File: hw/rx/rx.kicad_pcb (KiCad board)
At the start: 4 copper layers, 48 x 90 mm, 117 parts, among them J1 backplane 2x13, J2 SWD, J3 ANT_A, J4 ANT_B, J5 TO_MODULE, K1 TQ2SA-12V, Q1 BSS138, U1 BT40E, U2 PE4259, U3 PCM5102A, U4 TLV76733, U5 TLV76733, U6 OPA1656, U7 TPS3808G01

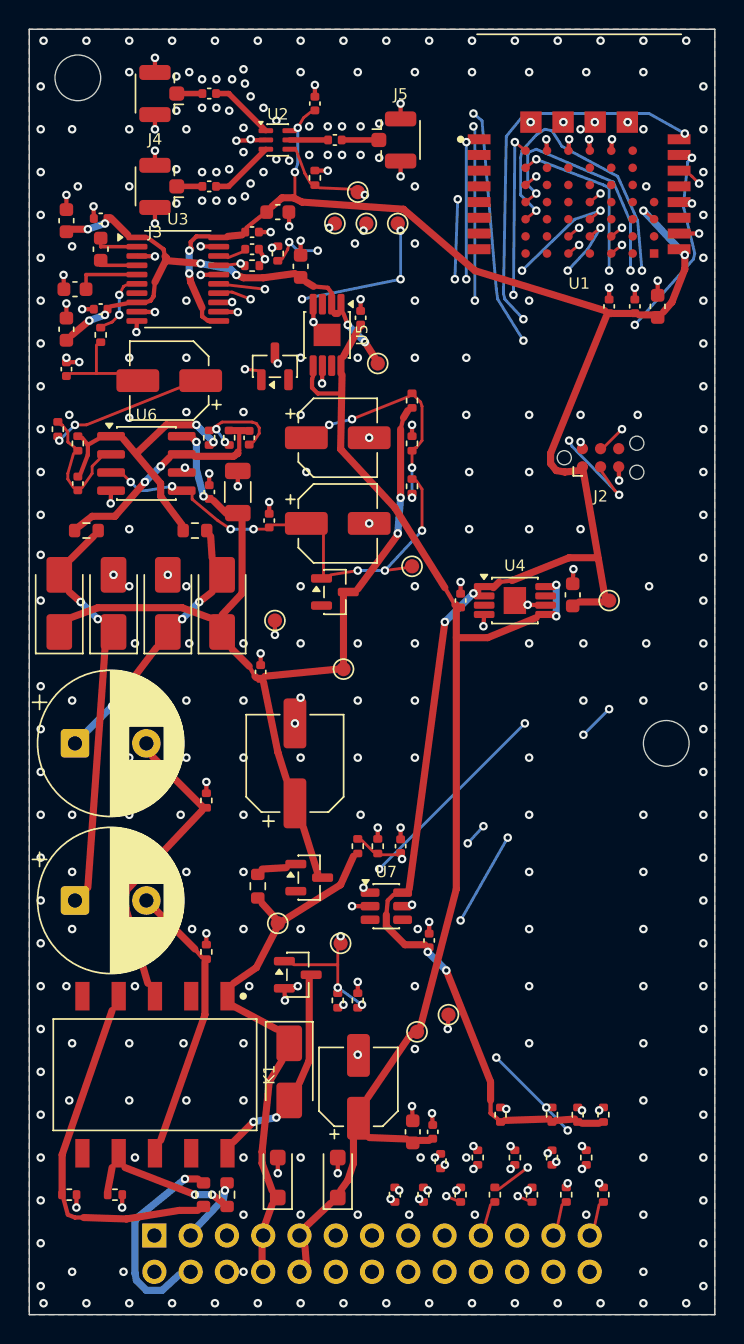
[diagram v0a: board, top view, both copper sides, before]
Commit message: hw/rx: field-solved 50 ohm GCPW, JLC rules that actually load (pack too), rx layout tests + CI (#34)
- rf_line.py: 2D quasi-static solve of the L1/L2 coplanar line; w 0.31 / gap 0.25 -> 50.1 ohm
  (the closed-form CPW formula misses by +7 ohm for gap > h)
- .kicad_dru: KiCad 10 drops the whole file on min_resolved_spokes; removed in pack and rx, guard tests added
- zone fill saved from kicad-cli (netclass RF gap reaches the gerbers)
- tests/test_rx_layout.py: DRC, rules loaded, fresh outputs, pad parity, RF width, current paths, analog keep-out,
  LCSC/DNP coverage, CPL rotations, mech record; CI pcb job runs it

Co-Authored-By: Claude Opus 5.5 <noreply@anthropic.com>
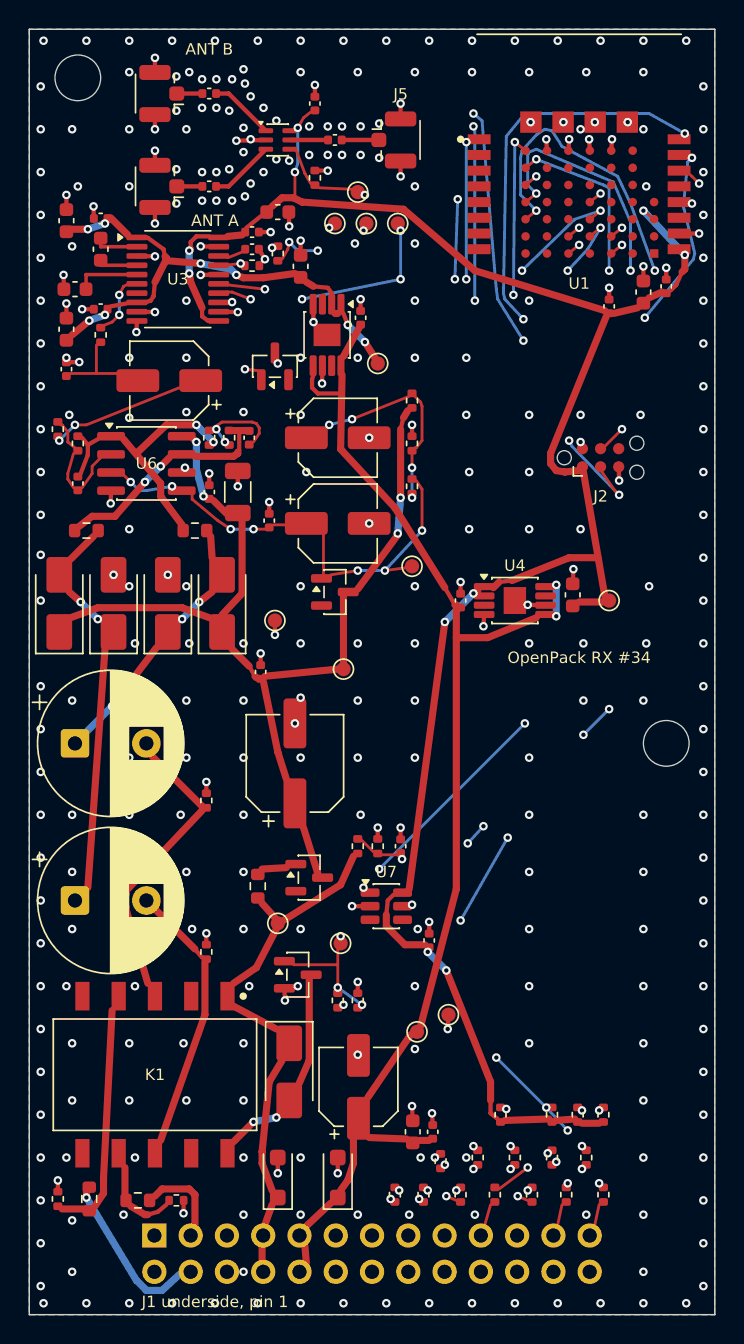
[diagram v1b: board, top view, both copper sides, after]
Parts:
- moved R48 8.01 mm to (104.2, 91.9)
- moved R51 6.26 mm to (107.6, 92.0), turned to 0 degrees
- moved R52 4.32 mm to (110.3, 92.0)
- moved C11 2.61 mm to (144.6, 28.0)
- moved C10 1.41 mm to (143.0, 28.4)
- moved R49 0.85 mm to (102.0, 91.9), turned to 90 degrees
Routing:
- net DRV_COLD_O: track 23.5 -> 15.4 mm
- net DRV_HOT_O: track 8.94 -> 4.78 mm, vias 2 -> 0
- net AUD_COLD: track 13.4 -> 10.9 mm
- net AUD_HOT: track 3.43 -> 5.27 mm, vias 1 -> 0
- net +3V3: track 131.8 -> 130.9 mm
- net GND: track 62.2 -> 62.1 mm, vias 334 -> 336
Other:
- board text added: "ANT A"
- board text added: "ANT B"
- board text added: "J1 underside, pin 1"
- board text added: "OpenPack RX #34"

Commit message: hw/rx: decoupling caps to their pins (op-amp V+ 1.9 mm, LDO in/out swapped to the right sides, supervisor) (#34)
Co-Authored-By: Claude Opus 5.5 <noreply@anthropic.com>
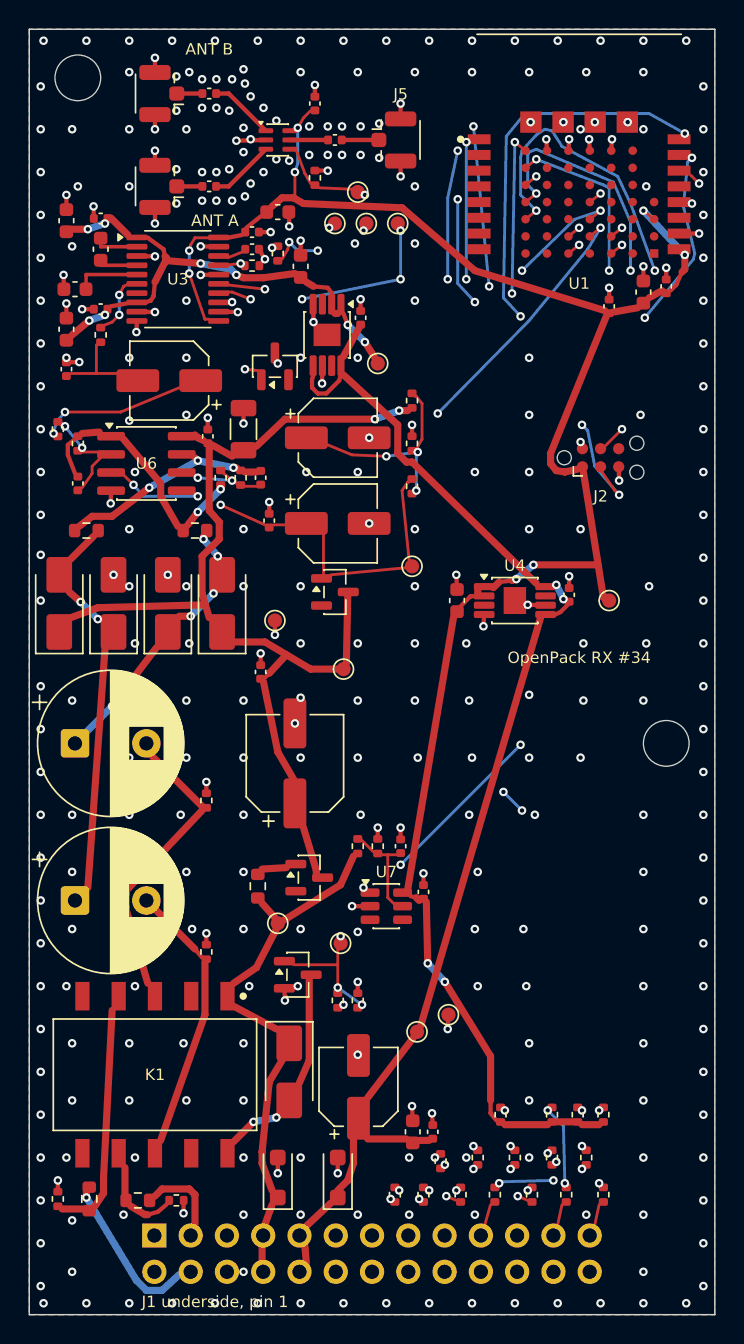
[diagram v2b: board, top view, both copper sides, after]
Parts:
- moved C4 8.11 mm to (129.9, 50.0)
- moved C3 7.61 mm to (137.8, 49.6)
- moved C46 4.42 mm to (115.0, 38.0)
- moved C45 3.90 mm to (112.5, 38.5)
- moved C61 3.42 mm to (127.6, 70.4)
- moved R43 2.91 mm to (113.4, 41.4)
- moved C42 2.91 mm to (116.2, 41.4)
- moved R44 2.91 mm to (114.8, 41.4)
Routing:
- net DRV_INB: track 9.55 -> 4.63 mm, vias 3 -> 2
- net +3V3: track 130.9 -> 126.5 mm
- net +5V: track 78.2 -> 75.1 mm
- net DRV_OUTA: track 17.8 -> 14.8 mm
- net nRESET: track 100.5 -> 103.4 mm, vias 8 -> 7
- net +12VA: track 59.0 -> 61.3 mm, vias 4 -> 2
- net DRV_INA: track 7.23 -> 5.97 mm, vias 0 -> 2
- net DRV_CIN: track 9.46 -> 10.2 mm
- net UART_TX: track 74.7 -> 74.0 mm, vias 5 -> 3
- net UART_RX: track 87.4 -> 86.8 mm, vias 6 -> 4
- net SLOT0: track 78.0 -> 77.4 mm
- net VCM: track 26.6 -> 26.0 mm, vias 7 -> 3
- net DRV_COLD_P: track 12.1 -> 12.6 mm, vias 3 -> 5
- net DRV_OUTB: track 13.8 -> 13.5 mm, vias 2 -> 3
- net VCM1: track 13.5 -> 13.4 mm, vias 4 -> 3
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
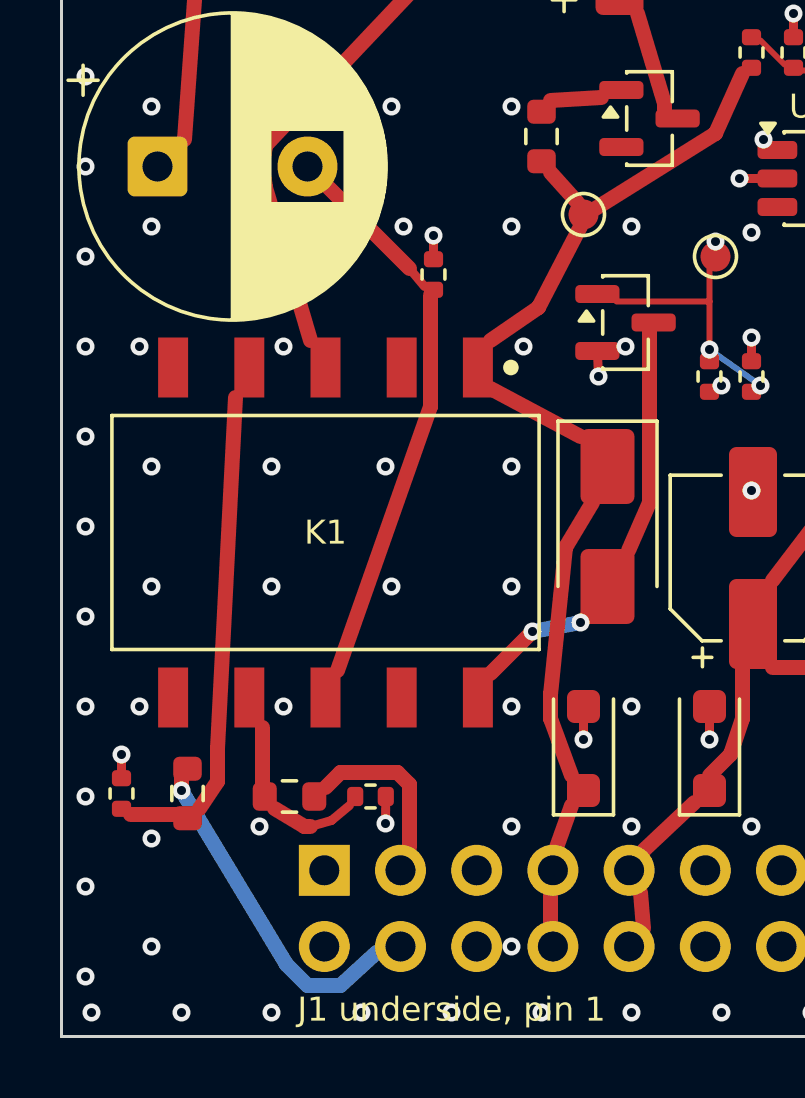
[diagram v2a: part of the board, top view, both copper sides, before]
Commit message: hw/rx: TQ2SA land pattern from the Panasonic datasheet, every LCSC code read from its record, C47/C48 height pinned (#34)
- TQ2SA SA type: 1.0 x 2.94 pads, 2.54 pitch, 9.56 row centres (TQ datasheet p.11)
- bom_jlc.csv: 39 placed lines, all codes checked on LCSC/JLC 2026-11-01 (17 former MATCH lines filled,
  relay now C2684447); only the BT40E consigned
- C47/C48 Nichicon UEP1J470MPD 10x16 (+1.5): 30.1 mm above the main board, mech.json + test

Co-Authored-By: Claude Opus 5.5 <noreply@anthropic.com>
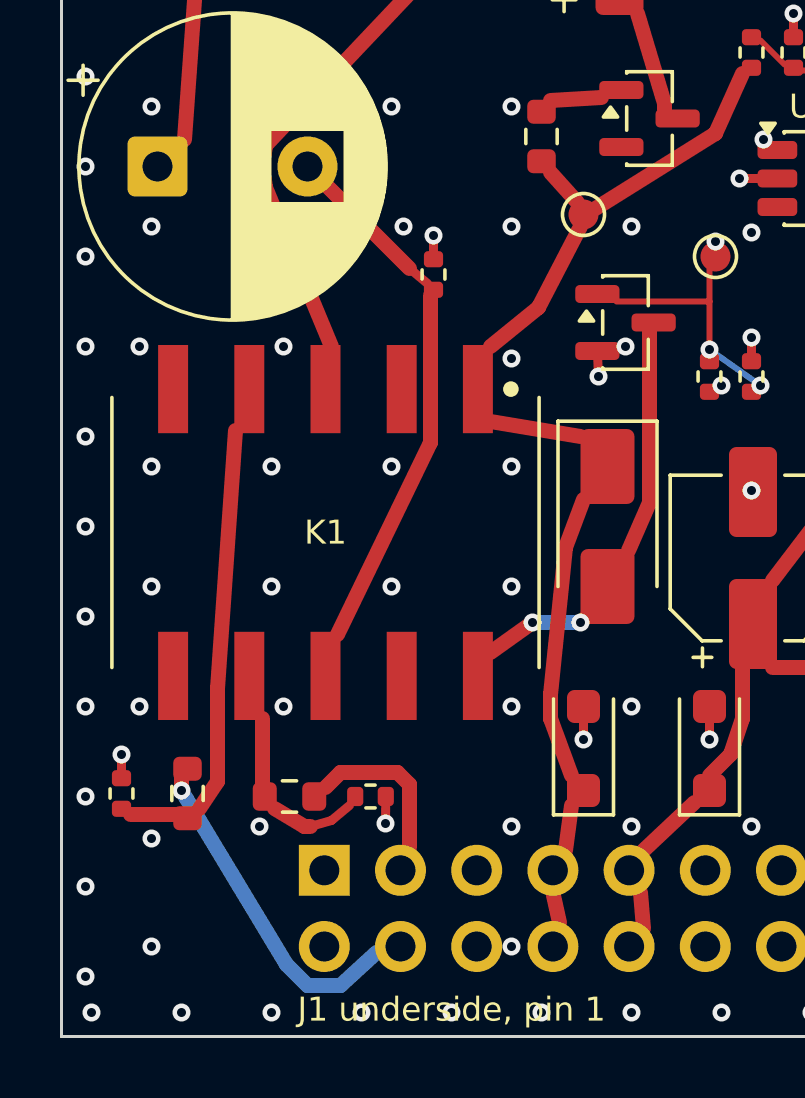
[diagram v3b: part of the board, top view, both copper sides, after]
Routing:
- net DRV_COLD_O: track 15.4 -> 14.3 mm
- net DRV_HOT_X: track 17.6 -> 16.6 mm

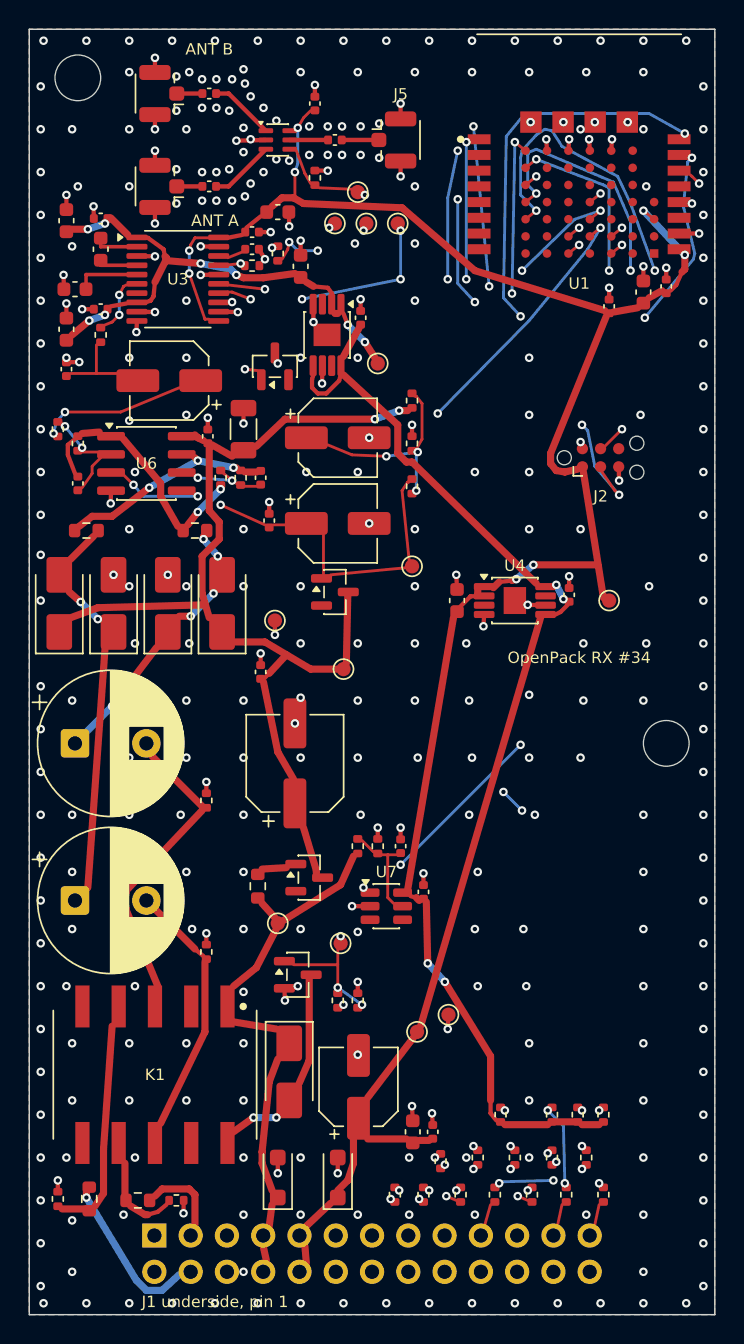
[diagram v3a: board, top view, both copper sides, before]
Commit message: hw/rx + hw/pack: #116 review fixes: netclass pour clearances (no 0.09 mm override), keyed J1 with no hole at 14, solid RF grounds, K1 pin-1/CPL rotation, raw RF numbers (#34)
- M1: JLC copper-clearance rule removed from rx and pack .kicad_dru; boards refilled/regenerated; probe-rule tests
  assert >= 0.125 mm everywhere and >= 0.15 mm to Audio_I on the committed fill; outer-copper rule width-independent
- S1: openpack:PinHeader_2x13_P2.54mm_Key14 (pad 14 deleted, KEY silk), header XFCN PZ254V-12-26P (LCSC C22465887,
  pin 14 cut), main-board socket Samtec SSW-113-01-G-D-14 recorded in ADR-0014; test
- S2: zone_connect solid on J3-J5, U2, U1 GND pads; test
- S3: TQ2SA pin-1 dot + '+', CPL +270 for the relay (K1 at 180); pin-1 marker + CPL test for all polarized parts
- N1 raw RF Z0 (51.5 bare / ~49.3 masked), N3 C44 at U6, REVIEW follow-ups

Co-Authored-By: Claude Opus 5.5 <noreply@anthropic.com>
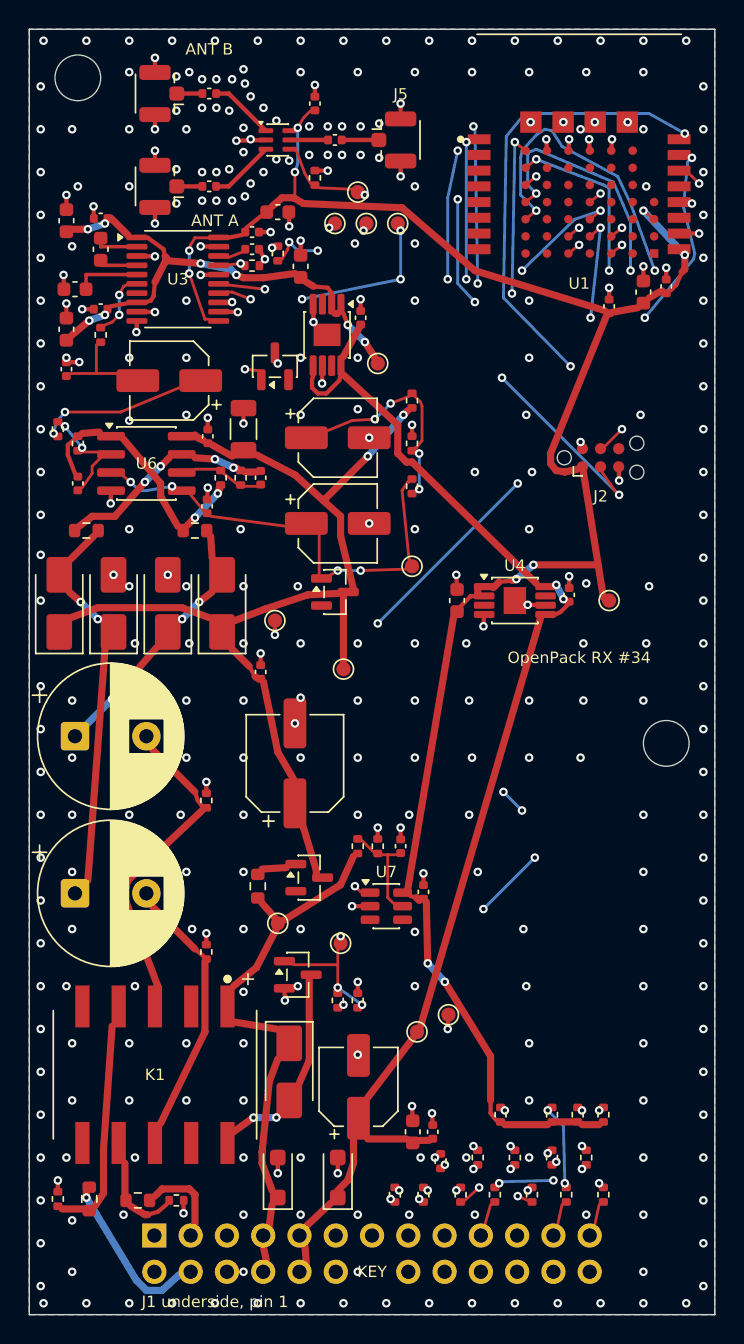
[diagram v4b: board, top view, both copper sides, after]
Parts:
- J1: footprint Connector_PinHeader_2.54mm:PinHeader_2x13_P2.54mm_Vertical -> openpack:PinHeader_2x13_P2.54mm_Key14
- moved C44 4.46 mm to (112.5, 43.4)
- moved C47 0.50 mm to (103.2, 59.5)
- moved C48 0.50 mm to (103.2, 70.5)
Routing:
- net UART_TX: track 74.0 -> 71.4 mm, vias 3 -> 5
- net +12VA: track 61.3 -> 58.9 mm
- net VCM: track 26.0 -> 24.6 mm, vias 3 -> 4
- net DRV_OUTB: track 13.5 -> 12.2 mm, vias 3 -> 4
- net DRV_INB: track 4.63 -> 3.44 mm, vias 2 -> 0
- net DRV_COLD_P: track 12.6 -> 11.7 mm, vias 5 -> 3
- net DRV_COLD_X: track 19.8 -> 20.4 mm
- net SWDIO: track 36.6 -> 37.2 mm
- net VCM1: vias 3 -> 4
- net GND: vias 339 -> 340
